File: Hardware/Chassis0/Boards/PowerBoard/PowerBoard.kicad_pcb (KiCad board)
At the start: 4 copper layers, 180 x 110 mm, 67 parts, among them IC1 ACS772ECB-400B-PFF-T, IC2 ACS772ECB-400B-PFF-T, IC3 ACS772ECB-400B-PFF-T, IC4 ACS772ECB-400B-PFF-T, J1 Conn_02x08_Counter_Clockwise, J2 7466205R, J3 7466205R, J4 7466205R, J5 Conn_02x08_Counter_Clockwise, J6 7466205R, J7 Conn_02x08_Counter_Clockwise, J8 7466205R, J9 Conn_02x08_Counter_Clockwise, Q1 IPB017N10N5ATMA1, Q10 IPB017N10N5ATMA1, Q11 IPB017N10N5ATMA1, Q12 IPB017N10N5ATMA1, Q2 IPB017N10N5ATMA1, Q3 IPB017N10N5ATMA1, Q4 IPB017N10N5ATMA1, Q5 IPB017N10N5ATMA1, Q6 IPB017N10N5ATMA1, Q7 IPB017N10N5ATMA1, Q8 IPB017N10N5ATMA1, Q9 IPB017N10N5ATMA1, U1 LMT87DCK

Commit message: Add power stage wip design for size 0
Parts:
- moved C12 14.0 mm to (38.0, 48.0), turned to 180 degrees
- moved C16 14.0 mm to (97.6, 48.0), turned to 180 degrees
- moved C20 13.4 mm to (158.1, 48.5), turned to 180 degrees
- moved C14 13.4 mm to (6.06, 48.0), turned to 0 degrees
- moved C18 13.0 mm to (65.4, 48.0), turned to 0 degrees
- moved C22 12.9 mm to (125.9, 48.0), turned to 0 degrees
- moved H10 11.5 mm to (160.5, 64.5)
- moved H8 11.0 mm to (99.5, 64.0)
- moved H6 11.0 mm to (40.0, 64.0)
- moved C13 9.05 mm to (6.06, 52.0), turned to 0 degrees
- moved C21 8.63 mm to (125.9, 52.0), turned to 0 degrees
- moved C17 8.58 mm to (65.4, 52.0), turned to 0 degrees
- moved C15 8.08 mm to (97.6, 53.5), turned to 180 degrees
- moved C11 8.00 mm to (38.0, 53.0), turned to 180 degrees
- moved C19 7.50 mm to (158.1, 53.5), turned to 180 degrees
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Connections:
- J9 pad 16: unconnected-(J9-Pin_16-Pad16) -> /NTC_C
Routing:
- net /DC_LINK_+: track 0.00 -> 194.9 mm, vias 0 -> 3
- net /GND_B: track 0.00 -> 188.9 mm, vias 0 -> 4
- net /+5V_B: track 0.00 -> 187.1 mm, vias 0 -> 4
- net /ISENSE_PH_U_B: track 0.00 -> 120.0 mm, vias 0 -> 2
- net /ISENSE_DC_LINK_B: track 0.00 -> 75.4 mm, vias 0 -> 4
- net /PH_V_H_G: track 0.00 -> 65.0 mm, vias 0 -> 4
- net /ISENSE_PH_V_B: track 0.00 -> 63.1 mm, vias 0 -> 2
- net /PH_U_H_G: track 0.00 -> 62.4 mm, vias 0 -> 4
- net /DC_LINK_-: track 0.00 -> 49.3 mm, vias 0 -> 630
- net /PHASE_V: track 0.00 -> 48.9 mm, vias 0 -> 1
- net /PHASE_U: track 0.00 -> 45.5 mm, vias 0 -> 1
- net /PH_W_H_G: track 0.00 -> 44.2 mm, vias 0 -> 2
- net /PHASE_W: track 0.00 -> 43.5 mm, vias 0 -> 1
- net /GND_C: track 0.00 -> 38.8 mm, vias 0 -> 2
- net /+5V_C: track 0.00 -> 32.4 mm, vias 0 -> 2
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- added copper zone on B.Cu, net Net-(IC2-IP+)
- added copper zone on F.Cu, net Net-(IC2-IP+)
- added copper zone on In1.Cu, net Net-(IC2-IP+)
- added copper zone on In2.Cu, net Net-(IC2-IP+)
- added copper zone on B.Cu, net Net-(IC3-IP+)
- added copper zone on F.Cu, net Net-(IC3-IP+)
- added copper zone on In1.Cu, net Net-(IC3-IP+)
- added copper zone on In2.Cu, net Net-(IC3-IP+)
- added copper zone on F.Cu, net Net-(IC4-IP+)
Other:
- board text added: "todo: move power to right side (both dc terminals are on right side) add ground planes maybe 2nd temp sense model+serial number variants and other info warning labels design authors (konstantin/thomas)"

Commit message: Update size 0 cad model
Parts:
- moved J6 6.98 mm to (116.0, 57.0)
- moved J4 6.12 mm to (55.0, 57.0)
- moved J3 2.83 mm to (170.0, 17.0)
- moved IC1 0.91 mm to (168.1, 51.8)
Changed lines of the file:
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@@
 	)
 	(footprint "Connector_PinHeader_2.54mm:PinHeader_2x08_P2.54mm_Vertical"
+		(locked yes)
 		(layer "F.Cu")
 		(at 72.76 107.54 90)
@@
 	)
 	(footprint "MountingHole:MountingHole_4.3mm_M4"
+		(locked yes)
 		(layer "F.Cu")
 		(at 160.5 64.5)
@@
 	(footprint "InverterCom:7466205R"
 		(layer "F.Cu")
-		(at 52 62.34)
+		(at 55 57)
 		(descr "7466205R-2")
 		(tags "Connector")
@@
 	)
 	(footprint "MountingHole:MountingHole_4.3mm_M4"
+		(locked yes)
 		(layer "F.Cu")
 		(at 121 82)
@@
 	)
 	(footprint "Connector_PinHeader_2.54mm:PinHeader_2x08_P2.54mm_Vertical"
+		(locked yes)
 		(layer "F.Cu")
 		(at 117.3 107.54 90)
@@
 	)
 	(footprint "MountingHole:MountingHole_4.3mm_M4"
+		(locked yes)
 		(layer "F.Cu")
 		(at 99.5 64)
@@
 	(footprint "InverterCom:7466205R"
 		(layer "F.Cu")
-		(at 111.5 62.34)
+		(at 116 57)
 		(descr "7466205R-2")
 		(tags "Connector")
@@
 	)
 	(footprint "Connector_PinHeader_2.54mm:PinHeader_2x08_P2.54mm_Vertical"
+		(locked yes)
 		(layer "F.Cu")
 		(at 13.76 107 90)
@@
 		)
 		(fp_text user "${REFERENCE}"
+			(locked yes)
 			(at 1.27 8.89 0)
 			(layer "F.Fab")
@@
 	)
 	(footprint "MountingHole:MountingHole_4.3mm_M4"
+		(locked yes)
 		(layer "F.Cu")
 		(at 61 82)
@@
 	(footprint "Sensor_Current:Allegro_CB_PFF"
 		(layer "F.Cu")
-		(at 168.09 52.74)
+		(at 168.09 51.825)
 		(descr "Allegro MicroSystems, CB-PFF Package (http://www.allegromicro.com/en/Products/Current-Sensor-ICs/Fifty-To-Two-Hundred-Amp-Integrated-Conductor-Sensor-ICs/ACS758.aspx) !PADS 4-5 DO NOT MATCH DATASHEET!")
 		(tags "Allegro CB-PFF")
@@
 	)
 	(footprint "Connector_PinHeader_2.54mm:PinHeader_2x08_P2.54mm_Vertical"
+		(locked yes)
 		(layer "F.Cu")
 		(at 149.38 107.275 90)
@@
 	)
 	(footprint "MountingHole:MountingHole_4.3mm_M4"
+		(locked yes)
 		(layer "F.Cu")
 		(at 40 64)
@@
 	(footprint "InverterCom:7466205R"
 		(layer "F.Cu")
-		(at 172 19)
+		(at 170 17)
 		(descr "7466205R-2")
 		(tags "Connector")
@@
 			(pts
 				(xy 20 0) (xy 5 15) (xy 0 15) (xy 0 45) (xy 0 40) (xy 0 46.5) (xy 0 50) (xy 10 60) (xy 35 60) (xy 45 50)
-				(xy 50 50) (xy 53.5 50) (xy 53.5 50) (xy 57.5 50) (xy 60 50) (xy 70 60) (xy 95 60) (xy 105 50) (xy 107.5 50)
+				(xy 50 50) (xy 53.5 50) (xy 57.5 50) (xy 60 50) (xy 70 60) (xy 95 60) (xy 105 50) (xy 107.5 50)
 				(xy 109 50) (xy 116.5 50) (xy 120 50) (xy 130 60) (xy 155 60) (xy 165 50.5) (xy 165 45) (xy 159.5 39.5)
 				(xy 155 35) (xy 155 0)
@@
 		(polygon
 			(pts
-				(xy 105 72) (xy 114 72) (xy 118 69) (xy 118 62) (xy 117 61) (xy 105 61)
+				(xy 105 59) (xy 105 76) (xy 115 76) (xy 121 70) (xy 121 55) (xy 119 53) (xy 111 53)
 			)
 		)
@@
 		(polygon
 			(pts
-				(xy 46 73) (xy 55 73) (xy 59 70) (xy 59 63) (xy 58 62) (xy 46 62)
+				(xy 46 57) (xy 46 73) (xy 55 73) (xy 59 70) (xy 59 54) (xy 57 52) (xy 51 52)
 			)
 		)
@@
 				(xy 10 94.418033) (xy 35 94.418033) (xy 35 59.418033) (xy 45 49.418033) (xy 60 49.418033) (xy 70 59.418033)
 				(xy 70 94.418033) (xy 95 94.418033) (xy 95 59.418033) (xy 105 49.418033) (xy 120 49.418033) (xy 130 59.418033)
-				(xy 130 94.418033) (xy 155 94.418033) (xy 155 59.418033) (xy 155 59.418033) (xy 165 49.918033) (xy 165 42.918033)
-				(xy 165 39.418033) (xy 170 33.418033) (xy 170 28.918033) (xy 160 19.418033) (xy 160 -0.581967)
+				(xy 130 94.418033) (xy 155 94.418033) (xy 155 59.418033) (xy 165 49.918033) (xy 165 42.918033) (xy 165 39.418033)
+				(xy 170 33.418033) (xy 170 28.918033) (xy 160 19.418033) (xy 160 -0.581967)
 			)
 		)

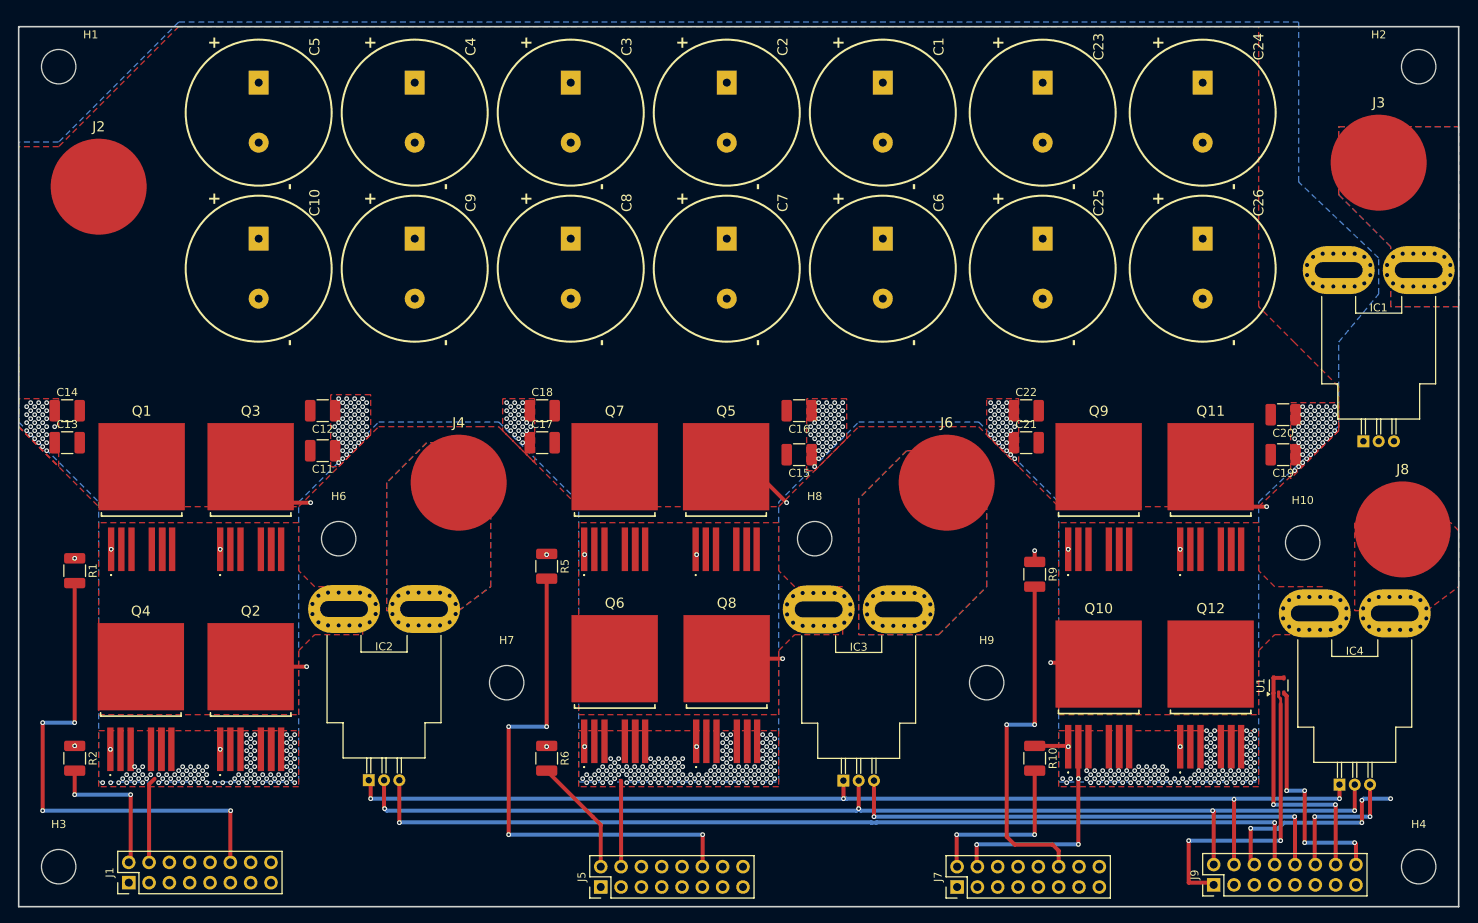
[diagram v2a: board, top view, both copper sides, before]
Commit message: Add control board outline for size 0
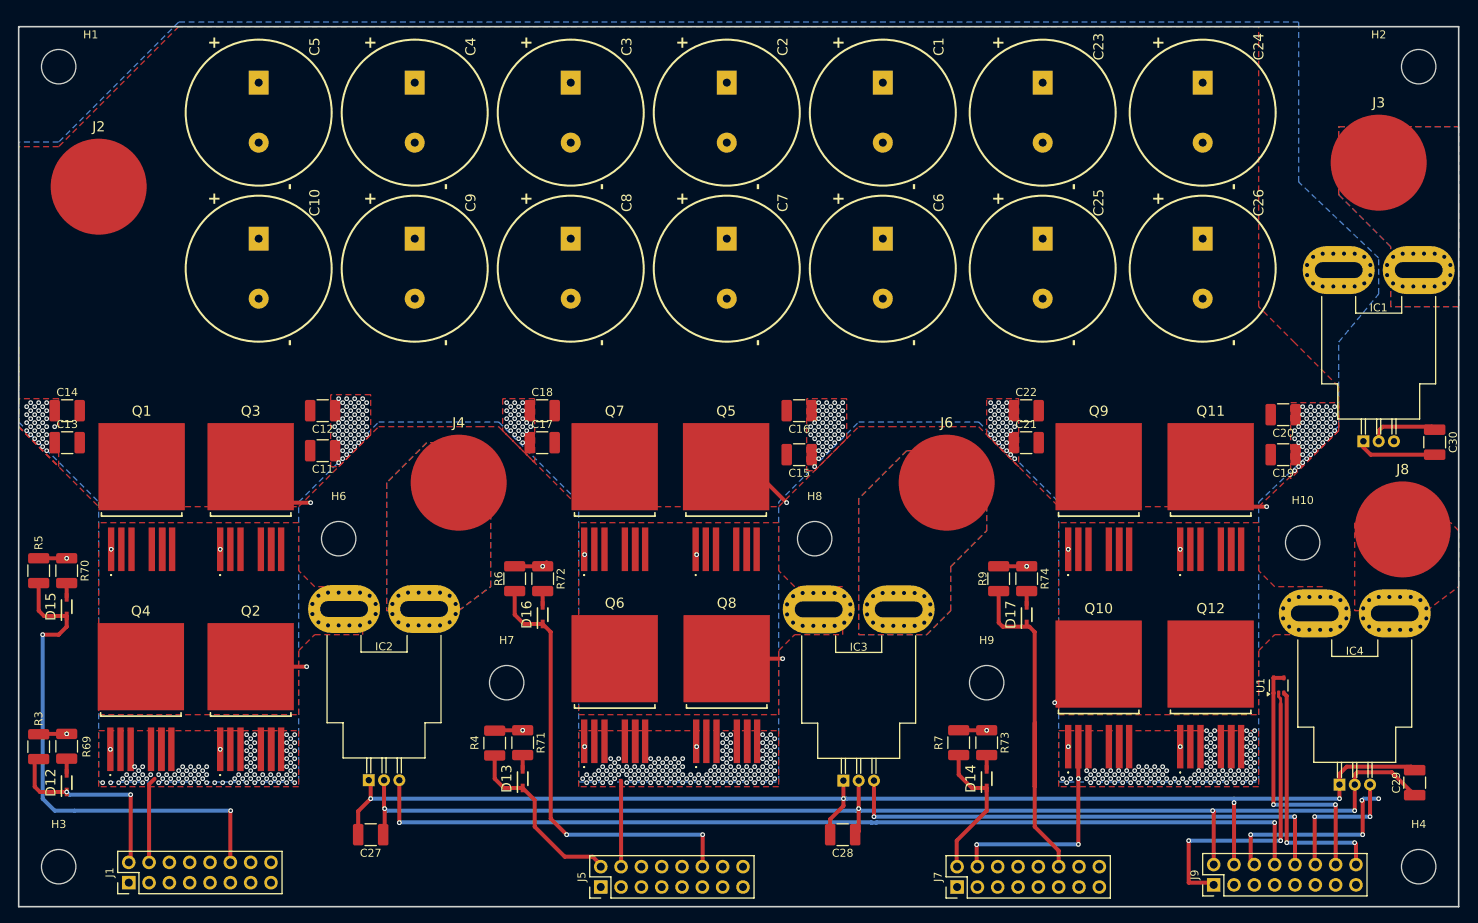
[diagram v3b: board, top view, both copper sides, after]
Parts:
- removed R1, R10, R2: 15, Resistor_SMD:R_1210_3225Metric_Pad1.30x2.65mm_HandSolder
- added C27: 100nF, Capacitor_SMD:C_1210_3225Metric_Pad1.33x2.70mm_HandSolder, F.Cu at (44.0, 101.0)
- added C28: 100nF, Capacitor_SMD:C_1210_3225Metric_Pad1.33x2.70mm_HandSolder, F.Cu at (103.0, 101.0)
- added C29: 100nF, Capacitor_SMD:C_1210_3225Metric_Pad1.33x2.70mm_HandSolder, F.Cu at (174.5, 94.5)
- added C30: 100nF, Capacitor_SMD:C_1210_3225Metric_Pad1.33x2.70mm_HandSolder, F.Cu at (177.0, 51.9)
- added D12: BAT54WS-7-F, InverterCom:SOD2513X120N, F.Cu at (6.00, 94.5)
- added D13: BAT54WS-7-F, InverterCom:SOD2513X120N, F.Cu at (63.0, 94.0)
- added D14: BAT54WS-7-F, InverterCom:SOD2513X120N, F.Cu at (121.0, 94.0)
- added D15: BAT54WS-7-F, InverterCom:SOD2513X120N, F.Cu at (6.00, 72.5)
- added D16: BAT54WS-7-F, InverterCom:SOD2513X120N, F.Cu at (65.5, 73.5)
- added D17: BAT54WS-7-F, InverterCom:SOD2513X120N, F.Cu at (126.0, 73.5)
- added R3: 9.6, Resistor_SMD:R_1210_3225Metric_Pad1.30x2.65mm_HandSolder, F.Cu at (2.50, 90.0)
- added R4: 9.6, Resistor_SMD:R_1210_3225Metric_Pad1.30x2.65mm_HandSolder, F.Cu at (59.5, 89.5)
- added R69: 6.8, Resistor_SMD:R_1210_3225Metric_Pad1.30x2.65mm_HandSolder, F.Cu at (6.00, 90.0)
- added R7: 9.6, Resistor_SMD:R_1210_3225Metric_Pad1.30x2.65mm_HandSolder, F.Cu at (117.5, 89.5)
- added R70: 6.8, Resistor_SMD:R_1210_3225Metric_Pad1.30x2.65mm_HandSolder, F.Cu at (6.00, 68.0)
- added R71: 6.8, Resistor_SMD:R_1210_3225Metric_Pad1.30x2.65mm_HandSolder, F.Cu at (63.0, 89.5)
- added R72: 6.8, Resistor_SMD:R_1210_3225Metric_Pad1.30x2.65mm_HandSolder, F.Cu at (65.5, 69.0)
- added R73: 6.8, Resistor_SMD:R_1210_3225Metric_Pad1.30x2.65mm_HandSolder, F.Cu at (121.0, 89.5)
- added R74: 6.8, Resistor_SMD:R_1210_3225Metric_Pad1.30x2.65mm_HandSolder, F.Cu at (126.0, 69.0)
- R5, R6, R9: value 15 -> 9.6
- moved R5 63.5 mm to (2.50, 68.0)
- moved R6 22.8 mm to (62.0, 69.0)
- moved R9 4.53 mm to (122.5, 69.0)
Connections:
- R5 pad 1: /HalfBridge1/HIGH_GATE -> /HalfBridge/HIGH_GATE
- R5 pad 2: /PH_V_H_G -> /PH_U_H_G
- R6 pad 1: /HalfBridge1/LOW_GATE -> /HalfBridge1/HIGH_GATE
- R6 pad 2: /PH_V_L_G -> /PH_V_H_G
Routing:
- net /+5V_B: track 187.1 -> 219.8 mm
- net /GND_B: track 188.9 -> 215.4 mm
- net /HalfBridge2/LOW_GATE: track 18.2 -> 28.7 mm, vias 2 -> 3
- net /PH_V_H_G: track 65.0 -> 55.5 mm, vias 4 -> 2
- net /PH_V_L_G: track 14.8 -> 22.8 mm
- net /HalfBridge1/LOW_GATE: track 18.8 -> 26.1 mm
- net /PH_U_L_G: track 18.6 -> 24.4 mm
- net /HalfBridge/LOW_GATE: track 18.4 -> 24.0 mm
- net /HalfBridge1/HIGH_GATE: track 18.8 -> 24.1 mm
- net /HalfBridge/HIGH_GATE: track 18.7 -> 23.2 mm
- net /HalfBridge2/HIGH_GATE: track 19.7 -> 23.6 mm
- net /PH_W_L_G: track 21.8 -> 18.1 mm, vias 2 -> 0
- net /PH_W_H_G: track 44.2 -> 47.5 mm, vias 2 -> 0
- net /PHASE_W: track 43.5 -> 40.7 mm
- net Net-(D12-A): track 0.00 -> 2.05 mm
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
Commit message: finish chassis 0 board design v1
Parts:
- moved C10 4.03 mm to (34.0, 26.0)
- moved C5 4.03 mm to (34.0, 6.50)
- moved C4 3.53 mm to (53.0, 6.50)
- moved C9 3.53 mm to (53.0, 26.0)
- moved C3 3.03 mm to (72.0, 6.50)
- moved C8 3.03 mm to (72.0, 26.0)
- moved C2 2.54 mm to (91.0, 6.50)
- moved C7 2.54 mm to (91.0, 26.0)
- moved C1 2.05 mm to (110.0, 6.50)
- moved C6 2.05 mm to (110.0, 26.0)
- moved C23 1.12 mm to (129.0, 6.50)
- moved C25 1.12 mm to (129.0, 26.0)
- moved C24 0.50 mm to (148.0, 6.50)
- moved C26 0.50 mm to (148.0, 26.0)
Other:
- board text added: "todo: add ground planes model+serial number variants and other info warning labels design authors (konstantin/thomas)"
- board text removed: "todo: move power to right side (both dc terminals are on right side) add ground planes maybe 2nd temp sense model+serial number variants and other info warning labels design authors (konstantin/thomas)"
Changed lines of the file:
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@@
 		(locked yes)
 		(layer "F.Cu")
-		(at 49.504 6.996 -90)
+		(at 53 6.504 -90)
 		(descr "18mm x 30.5mm")
 		(tags "Capacitor")
@@
 		(locked yes)
 		(layer "F.Cu")
-		(at 69.008 6.996 -90)
+		(at 72 6.504 -90)
 		(descr "18mm x 30.5mm")
 		(tags "Capacitor")
@@
 		(locked yes)
 		(layer "F.Cu")
-		(at 128 26.5 -90)
+		(at 129 26.004 -90)
 		(descr "18mm x 30.5mm")
 		(tags "Capacitor")
@@
 		(locked yes)
 		(layer "F.Cu")
-		(at 148 26.5 -90)
+		(at 148 26.004 -90)
 		(descr "18mm x 30.5mm")
 		(tags "Capacitor")
@@
 		(locked yes)
 		(layer "F.Cu")
-		(at 148 7 -90)
+		(at 148 6.504 -90)
 		(descr "18mm x 30.5mm")
 		(tags "Capacitor")
@@
 		(locked yes)
 		(layer "F.Cu")
-		(at 108.016 6.996 -90)
+		(at 110 6.5 -90)
 		(descr "18mm x 30.5mm")
 		(tags "Capacitor")
@@
 		(locked yes)
 		(layer "F.Cu")
-		(at 30 26.5 -90)
+		(at 34 26.008 -90)
 		(descr "18mm x 30.5mm")
 		(tags "Capacitor")
@@
 		(locked yes)
 		(layer "F.Cu")
-		(at 88.512 26.5 -90)
+		(at 91 26.004 -90)
 		(descr "18mm x 30.5mm")
 		(tags "Capacitor")
@@
 		(locked yes)
 		(layer "F.Cu")
-		(at 128 7 -90)
+		(at 129 6.504 -90)
 		(descr "18mm x 30.5mm")
 		(tags "Capacitor")
@@
 		(locked yes)
 		(layer "F.Cu")
-		(at 108.016 26.5 -90)
+		(at 110 26.004 -90)
 		(descr "18mm x 30.5mm")
 		(tags "Capacitor")
@@
 		(locked yes)
 		(layer "F.Cu")
-		(at 88.512 6.996 -90)
+		(at 91 6.5 -90)
 		(descr "18mm x 30.5mm")
 		(tags "Capacitor")
@@
 		(locked yes)
 		(layer "F.Cu")
-		(at 49.504 26.5 -90)
+		(at 53 26.008 -90)
 		(descr "18mm x 30.5mm")
 		(tags "Capacitor")
@@
 		(locked yes)
 		(layer "F.Cu")
-		(at 30 6.996 -90)
+		(at 34 6.504 -90)
 		(descr "18mm x 30.5mm")
 		(tags "Capacitor")
@@
 		(locked yes)
 		(layer "F.Cu")
-		(at 69.008 26.5 -90)
+		(at 72 26.008 -90)
 		(descr "18mm x 30.5mm")
 		(tags "Capacitor")
@@
 		(layer "Edge.Cuts")
 	)
-	(gr_text "todo:\nmove power to right side (both dc terminals are on right side)\nadd ground planes\nmaybe 2nd temp sense\nmodel+serial number\nvariants and other info\nwarning labels\ndesign authors (konstantin/thomas)"
+	(gr_text "todo:\nadd ground planes\nmodel+serial number\nvariants and other info\nwarning labels\ndesign authors (konstantin/thomas)"
 		(at 181 -2 0)
 		(layer "Edge.Cuts")
@@
 		(polygon
 			(pts
-				(xy 20 -0.581967) (xy 5 14.418033) (xy 0 14.418033) (xy 0 44.418033) (xy 0 49.418033) (xy 10 59.418033)
-				(xy 10 94.418033) (xy 35 94.418033) (xy 35 59.418033) (xy 45 49.418033) (xy 60 49.418033) (xy 70 59.418033)
-				(xy 70 94.418033) (xy 95 94.418033) (xy 95 59.418033) (xy 105 49.418033) (xy 120 49.418033) (xy 130 59.418033)
-				(xy 130 94.418033) (xy 155 94.418033) (xy 155 59.418033) (xy 165 49.918033) (xy 165 42.918033) (xy 165 39.418033)
-				(xy 170 33.418033) (xy 170 28.918033) (xy 160 19.418033) (xy 160 -0.581967)
+				(xy 20.040984 -0.040984) (xy 5.040984 14.959016) (xy 0.040984 14.959016) (xy 0.040984 44.959016)
+				(xy 0.040984 49.959016) (xy 10.040984 59.959016) (xy 10.040984 94.959016) (xy 35.040984 94.959016)
+				(xy 35.040984 59.959016) (xy 45.040984 49.959016) (xy 60.040984 49.959016) (xy 70.040984 59.959016)
+				(xy 70.040984 94.959016) (xy 95.040984 94.959016) (xy 95.040984 59.959016) (xy 105.040984 49.959016)
+				(xy 120.040984 49.959016) (xy 130.040984 59.959016) (xy 130.040984 94.959016) (xy 155.040984 94.959016)
+				(xy 155.040984 59.959016) (xy 165.040984 50.459016) (xy 165.040984 43.459016) (xy 165.040984 39.959016)
+				(xy 170.040984 33.959016) (xy 170.040984 29.459016) (xy 160.040984 19.959016) (xy 160.040984 -0.040984)
 			)
 		)
